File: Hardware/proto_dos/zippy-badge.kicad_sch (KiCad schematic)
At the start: 46 parts, among them J1 Micro_SD_Card_SPI, J2 USB-C, SW1 Boot Select, SW2 SW_SPDT, SW3 SKRHABE010, U1 NCP115ASN330T2G, U2 RP2040, U3 W25Q32RV, U4 GSDA213, X1 Badgelife_sao_connector_v169b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, Y1 ABM8-272-T3

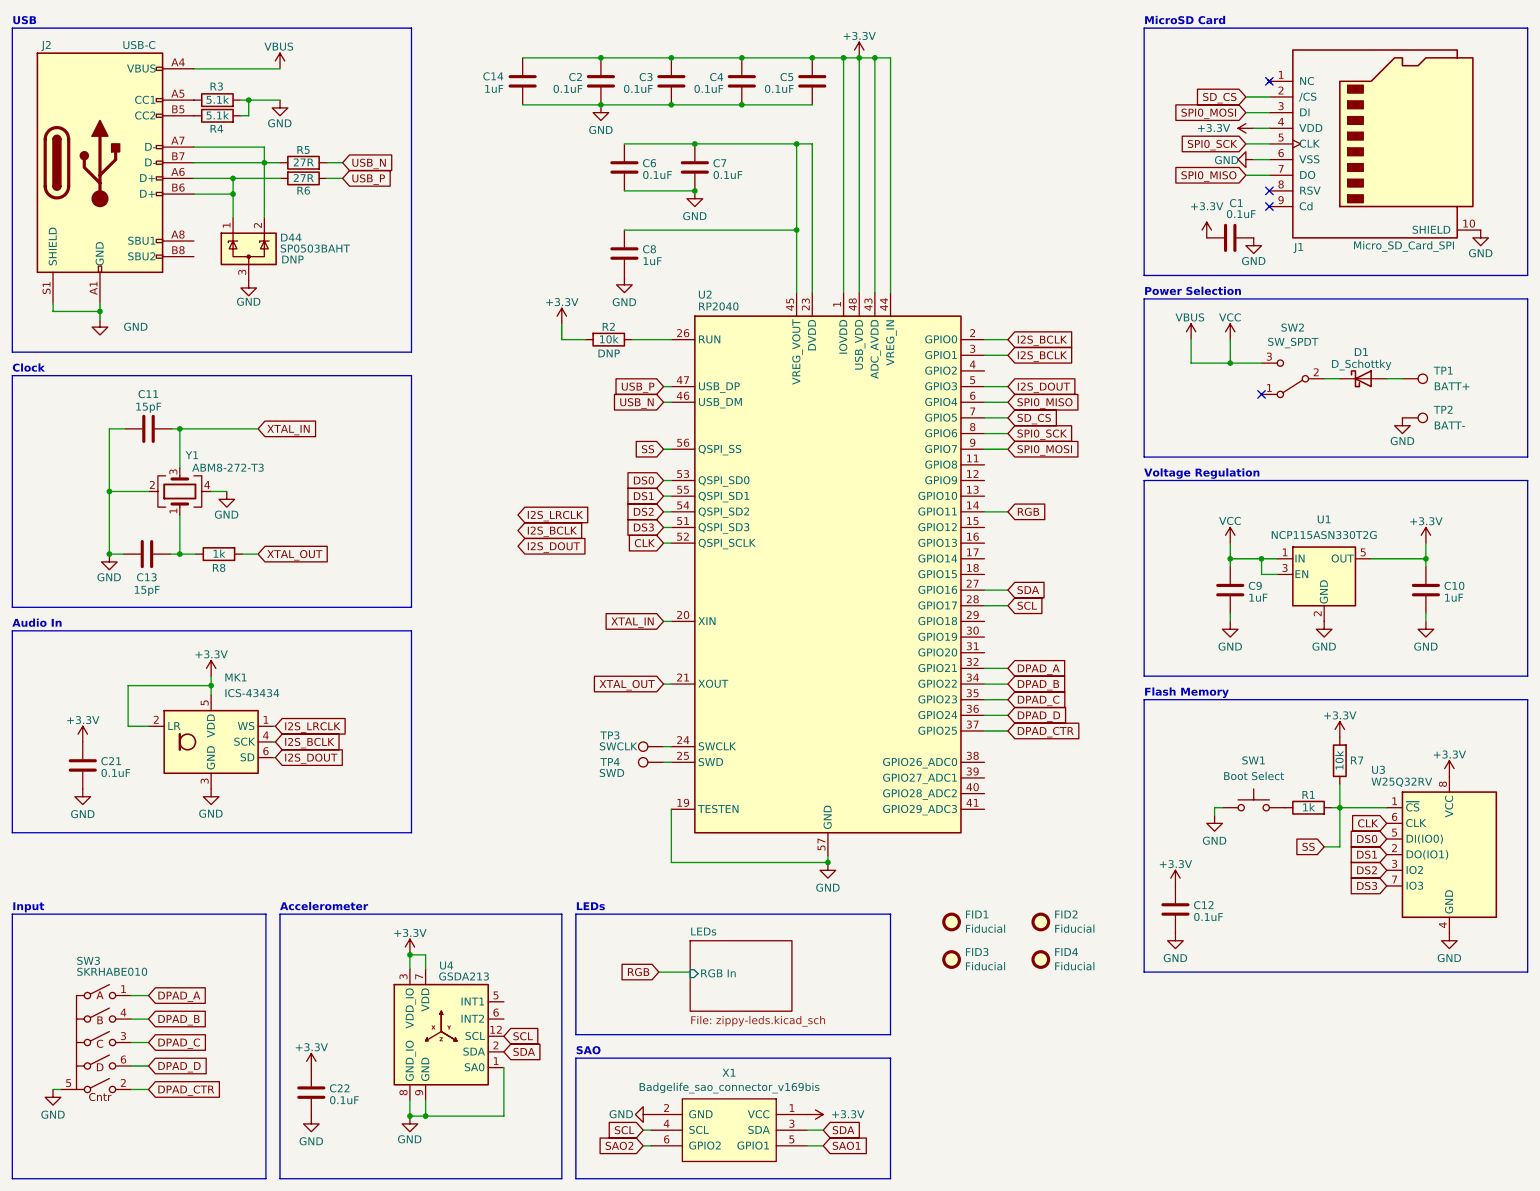
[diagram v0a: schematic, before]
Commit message: Updated schematic to add Flipper Zero GPIO pinout Modified pin out of RP2040 to make for better routing Update of PCB to add new parts and test layout
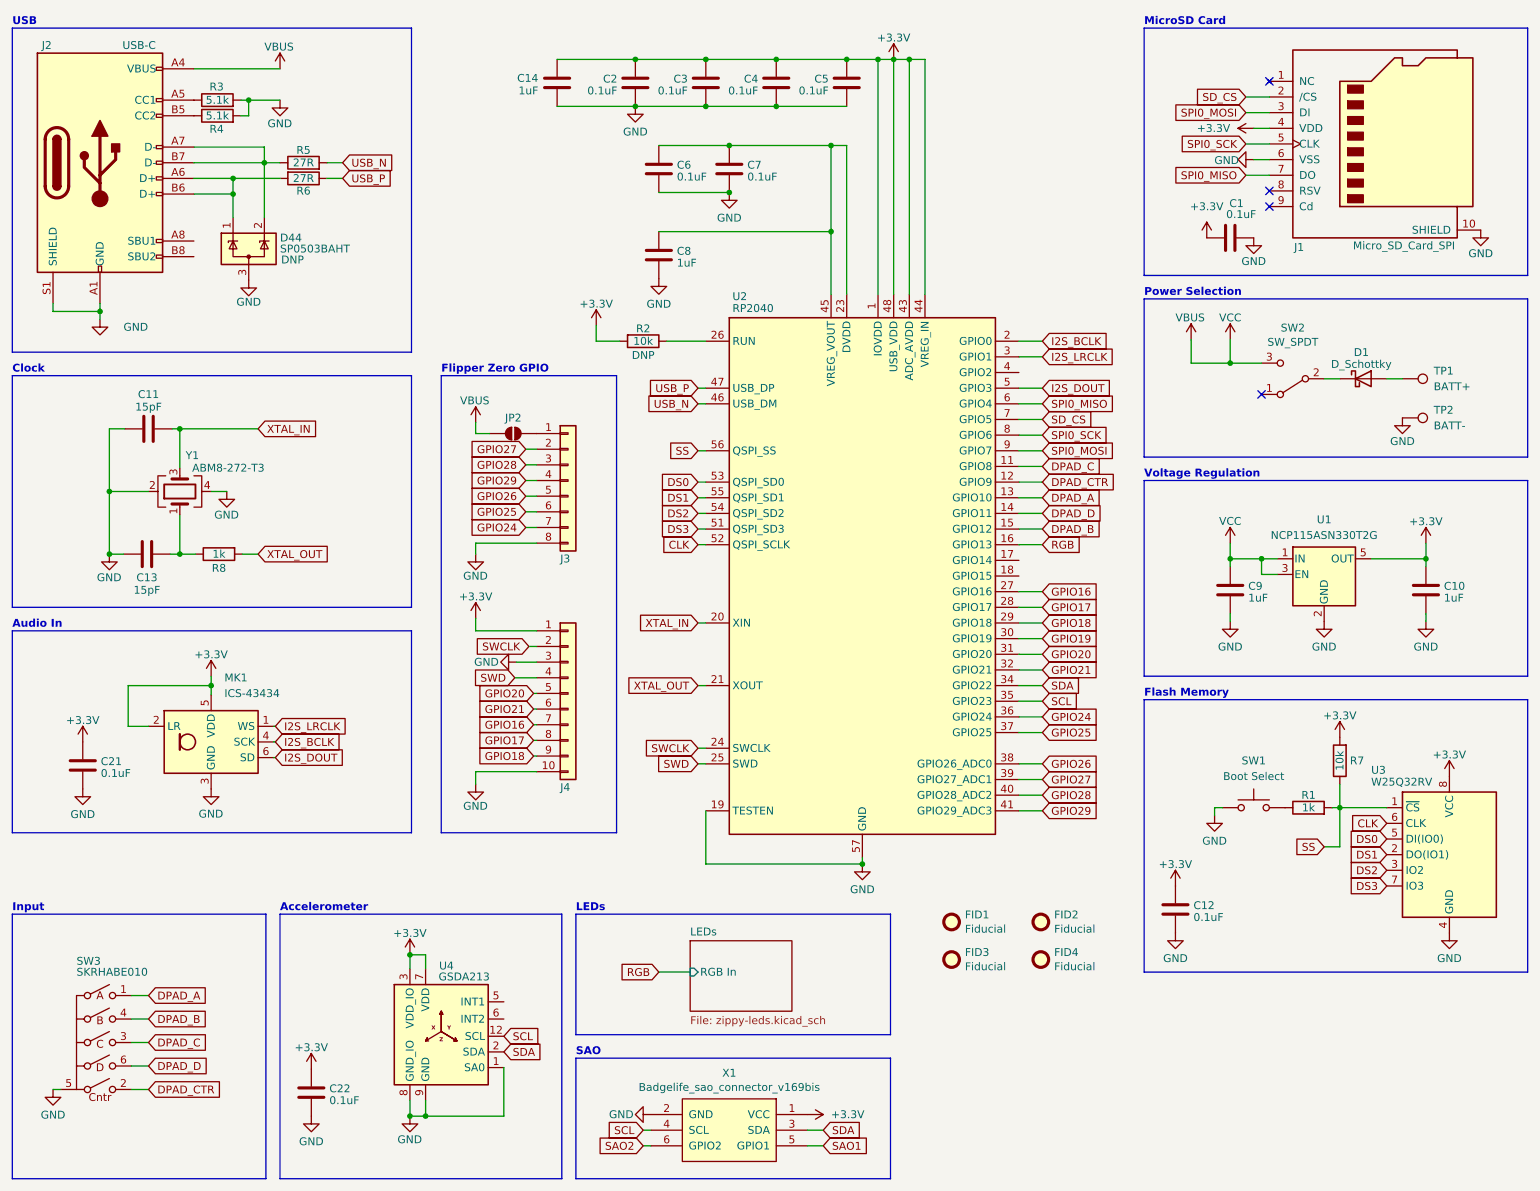
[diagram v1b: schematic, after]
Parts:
- removed TP3: SWCLK, TestPoint:TestPoint_Pad_2.5x2.5mm, symbol Connector:TestPoint
- removed TP4: SWD, TestPoint:TestPoint_Pad_2.5x2.5mm, symbol Connector:TestPoint
- added J3: Conn_01x08, Connector_PinHeader_2.54mm:PinHeader_1x08_P2.54mm_Vertical, symbol Connector_Generic:Conn_01x08
- added J4: Conn_01x10, Connector_PinHeader_2.54mm:PinHeader_1x10_P2.54mm_Vertical, symbol Connector_Generic:Conn_01x10
- added JP2: SolderJumper_2_Open, Jumper:SolderJumper-2_P1.3mm_Open_RoundedPad1.0x1.5mm, symbol Jumper:SolderJumper_2_Open
- SW3: footprint (none) -> lib_fp:SKRHABE010
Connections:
- net +3.3V: now also J4.1 (Pin_1)
- net DPAD_A: now also U2.13 (GPIO10); no longer U2.32 (GPIO21)
- net DPAD_B: now also U2.15 (GPIO12); no longer U2.34 (GPIO22)
- net DPAD_C: now also U2.11 (GPIO8); no longer U2.35 (GPIO23)
- net DPAD_CTR: now also U2.12 (GPIO9); no longer U2.37 (GPIO25)
- net DPAD_D: now also U2.14 (GPIO11); no longer U2.36 (GPIO24)
- net GND: now also J3.8 (Pin_8), J4.10 (Pin_10), J4.3 (Pin_3)
- net I2S_BCLK: no longer U2.3 (GPIO1)
- net I2S_LRCLK: now also U2.3 (GPIO1)
- net RGB: now also U2.16 (GPIO13); no longer U2.14 (GPIO11)
- net SCL: now also U2.35 (GPIO23); no longer U2.28 (GPIO17)
- net SDA: now also U2.34 (GPIO22); no longer U2.27 (GPIO16)
- net VBUS: now also JP2.1 (A)
- net SWCLK: now reaches U2.24 (SWCLK)
- net SWCLK: now also J4.2 (Pin_2)
- net SWD: now reaches U2.25 (SWD)
- net SWD: now also J4.4 (Pin_4)
- net GPIO18: now reaches U2.29 (GPIO18)
- net GPIO18: now also J4.9 (Pin_9)
- net GPIO19: now reaches U2.30 (GPIO19)
- net GPIO20: now reaches U2.31 (GPIO20)
- net GPIO20: now also J4.5 (Pin_5)
- net GPIO26: now reaches U2.38 (GPIO26_ADC0)
- net GPIO26: now also J3.5 (Pin_5)
- net GPIO27: now reaches U2.39 (GPIO27_ADC1)
- net GPIO27: now also J3.2 (Pin_2)
- net GPIO28: now reaches U2.40 (GPIO28_ADC2)
- net GPIO28: now also J3.3 (Pin_3)
- net GPIO29: now reaches U2.41 (GPIO29_ADC3)
- net GPIO29: now also J3.4 (Pin_4)
- new net: J3.1 (Pin_1), JP2.2 (B)
- new net GPIO16: J4.7 (Pin_7), U2.27 (GPIO16)
- new net GPIO17: J4.8 (Pin_8), U2.28 (GPIO17)
- new net GPIO21: J4.6 (Pin_6), U2.32 (GPIO21)
- new net GPIO24: J3.7 (Pin_7), U2.36 (GPIO24)
- new net GPIO25: J3.6 (Pin_6), U2.37 (GPIO25)
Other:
- note added: "Flipper Zero GPIO"
- moved on the sheet: C14, C2, C3, C4, C5, C6, C7, C8, R2, U2

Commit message: Updating artwork outlines to remove complexity at the bottom Adding 3D files for parts Adding STEP file for board Adding SolidWorks assembly for badge with shell
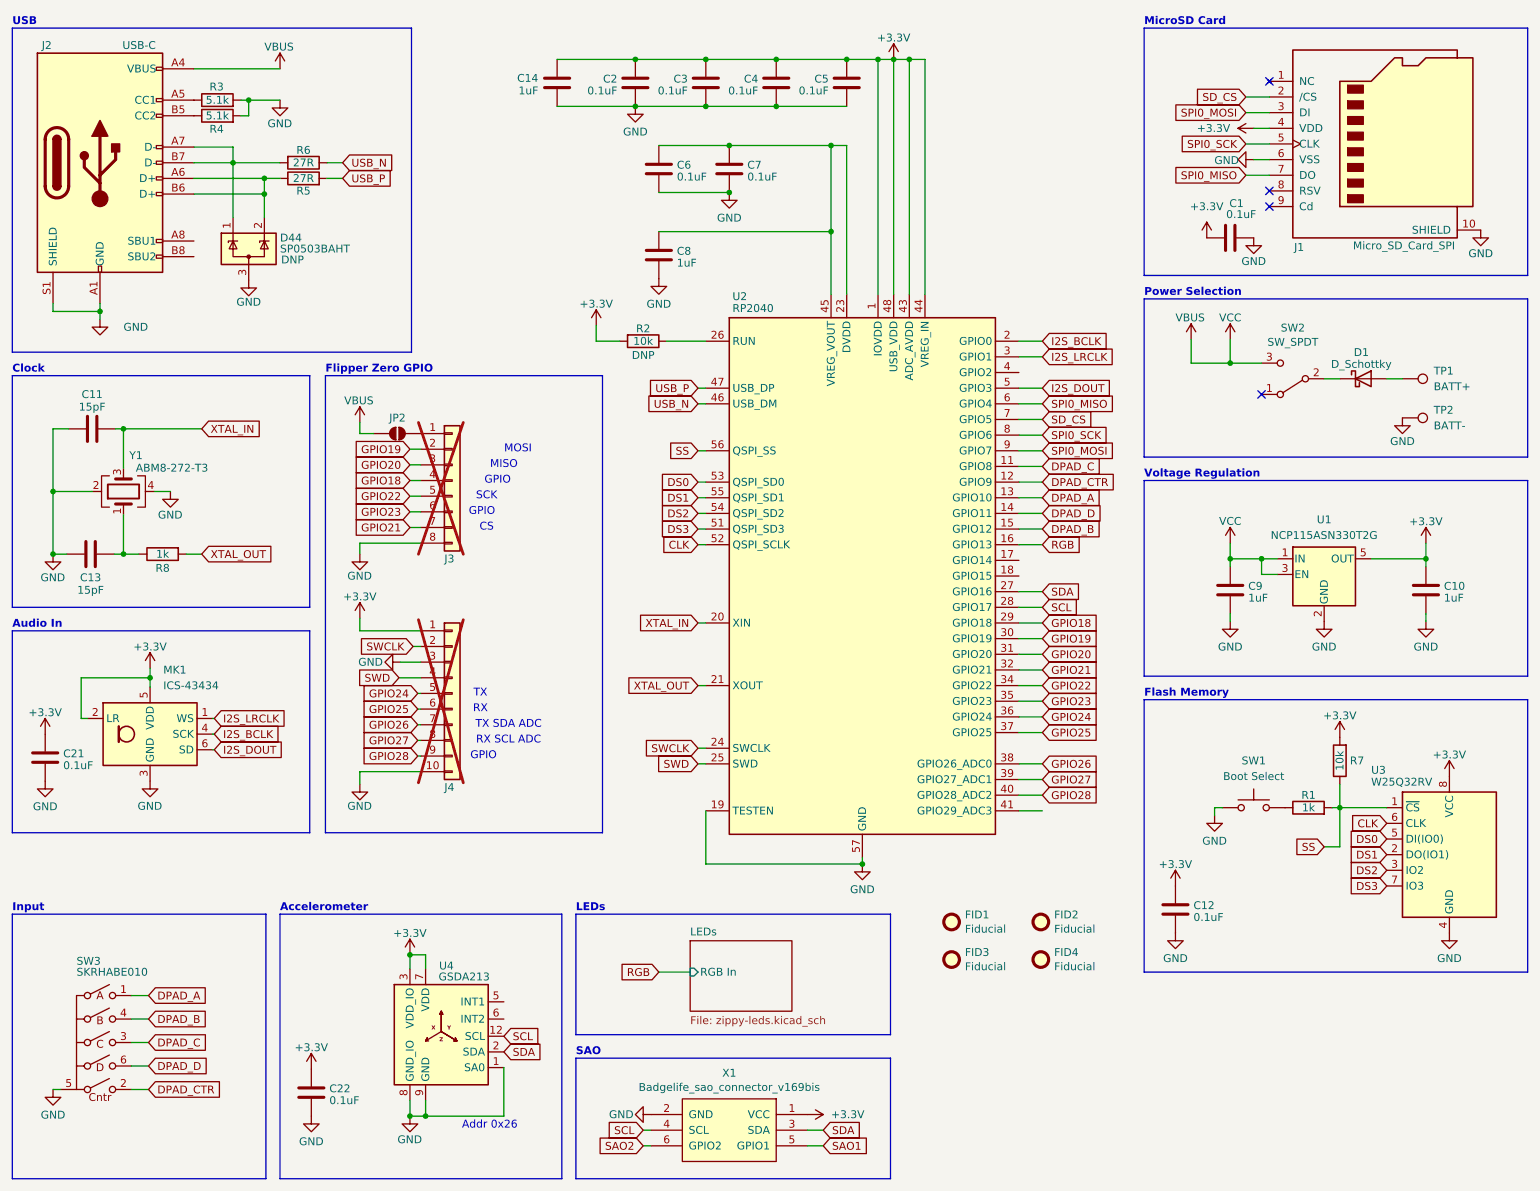
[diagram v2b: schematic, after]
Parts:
- D1: footprint Diode_SMD:D_SOD-523 -> Diode_SMD:D_SOD-123F
- J3, J4: now not fitted
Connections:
- net GPIO18: now also J3.4 (Pin_4); no longer J4.9 (Pin_9)
- net GPIO19: now also J3.2 (Pin_2)
- net GPIO20: now also J3.3 (Pin_3); no longer J4.5 (Pin_5)
- net GPIO21: now also J3.7 (Pin_7); no longer J4.6 (Pin_6)
- net GPIO24: now also J4.5 (Pin_5); no longer J3.7 (Pin_7)
- net GPIO25: now also J4.6 (Pin_6); no longer J3.6 (Pin_6)
- net GPIO26: now also J4.7 (Pin_7); no longer J3.5 (Pin_5)
- net GPIO27: now also J4.8 (Pin_8); no longer J3.2 (Pin_2)
- net GPIO28: now also J4.9 (Pin_9); no longer J3.3 (Pin_3)
- net SCL: now also U2.28 (GPIO17); no longer U2.35 (GPIO23)
- net SDA: now also U2.27 (GPIO16); no longer U2.34 (GPIO22)
- net USB_N: now also R6.1; no longer R5.2
- net USB_P: now also R5.2; no longer R6.1
- net at D44.1 (K), R6.2: now also J2.A7 (D-), J2.B7 (D-); no longer J2.A6 (D+), J2.B6 (D+)
- net at D44.2 (K), R5.1: now also J2.A6 (D+), J2.B6 (D+); no longer J2.A7 (D-), J2.B7 (D-)
- removed net GPIO16: J4.7 (Pin_7), U2.27 (GPIO16)
- removed net GPIO17: J4.8 (Pin_8), U2.28 (GPIO17)
- net GPIO29: no longer names the net of U2.41 (GPIO29_ADC3)
- net GPIO29: no longer J3.4 (Pin_4)
- new net GPIO22: J3.5 (Pin_5), U2.34 (GPIO22)
- new net GPIO23: J3.6 (Pin_6), U2.35 (GPIO23)
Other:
- note added: "Addr 0x26"
- note added: "CS"
- note added: "GPIO"
- note added: "MISO"
- note added: "MOSI"
- note added: "RX"
- note added: "RX SCL ADC"
- note added: "SCK"
- note added: "TX"
- note added: "TX SDA ADC"
- moved on the sheet: C11, C13, C21, JP2, MK1, R5, R6, R8, Y1
